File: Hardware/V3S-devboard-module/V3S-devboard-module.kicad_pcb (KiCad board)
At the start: 4 copper layers, 31.9 x 52.9 mm, 84 parts, among them J101 Conn_01x02, J201 Micro_SD_Card_Det1, J301 AS0BC21-S30BE-7H, SW201 SW_MEC_5E, U101 EA3036C, U102 XC6206PxxxMR, U201 V3S, U202 W25Q128JVS, Y201 Crystal_Small, Y202 Crystal_GND24_Small

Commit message: started working on exp board
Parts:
- moved J101 153.1 mm to (6.64, 2.68)
- moved C103 148.6 mm to (21.5, 15.2)
- moved C104 148.6 mm to (21.5, 13.5)
- moved C105 148.6 mm to (25.7, 18.0)
- moved C108 148.6 mm to (21.5, 10.5)
- moved C109 148.6 mm to (20.4, 8.68)
- moved C111 148.6 mm to (26.4, 8.57)
- moved C202 148.6 mm to (24.4, 34.8)
- moved C203 148.6 mm to (19.0, 30.5)
- moved C204 148.6 mm to (20.1, 31.6)
- moved C207 148.6 mm to (20.8, 32.9)
- moved C208 148.6 mm to (18.4, 36.8)
- moved C210 148.6 mm to (16.8, 34.4)
- moved C211 148.6 mm to (16.1, 33.7)
- moved C213 148.6 mm to (12.5, 41.0)
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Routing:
- net 5V: track 41.3 -> 45.0 mm
- net 1V2: track 179.8 -> 178.9 mm
- net GND: vias 54 -> 95
- net (no net): vias 1 -> 0
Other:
- board size 31.9 x 52.9 mm -> 32 x 55 mm

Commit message: working on final touches
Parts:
- added D101: LED, LED_SMD:LED_0603_1608Metric, F.Cu at (25.2, 2.27)
- added R108: 1K, Resistor_SMD:R_0402_1005Metric, B.Cu at (27.8, 2.27)
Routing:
- net Net-(D101-A): track 0.00 -> 2.82 mm, vias 0 -> 1
- net 5V: vias 38 -> 39
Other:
- board text added: "AM 2k24"
- board text added: "V3S Devboard"

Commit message: Minor changes. Sent to fab
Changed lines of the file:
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@@
 	)
 	(via
-		(at 19.138119 36.036881)
+		(at 19.3 35.9)
 		(size 0.5)
 		(drill 0.3)
@@
 		(start 10.275 39.875)
 		(end 8.925 39.875)
+		(width 0.5)
+		(layer "In1.Cu")
+		(net 2)
+	)
+	(segment
+		(start 13.325 41.85)
+		(end 9.475 41.85)
+		(width 0.5)
+		(layer "In1.Cu")
+		(net 2)
+	)
+	(segment
+		(start 19.275 35.9)
+		(end 13.325 41.85)
 		(width 0.5)
 		(layer "In1.Cu")
@@
 	)
 	(segment
-		(start 8.125 40.5)
-		(end 9.475 41.85)
+		(start 9.475 41.85)
+		(end 8.125 40.5)
 		(width 0.5)
 		(layer "In1.Cu")
@@
 	)
 	(segment
-		(start 7.575 40.5)
-		(end 2.9 35.825)
+		(start 19.3 35.9)
+		(end 19.275 35.9)
 		(width 0.5)
 		(layer "In1.Cu")
@@
 	)
 	(segment
-		(start 13.325 41.85)
-		(end 19.138119 36.036881)
+		(start 7.575 40.5)
+		(end 2.9 35.825)
 		(width 0.5)
 		(layer "In1.Cu")
@@
 		(width 0.5)
 		(layer "In1.Cu")
-		(net 2)
-	)
-	(segment
-		(start 9.475 41.85)
-		(end 13.325 41.85)
-		(width 0.5)
-		(layer "In1.Cu")

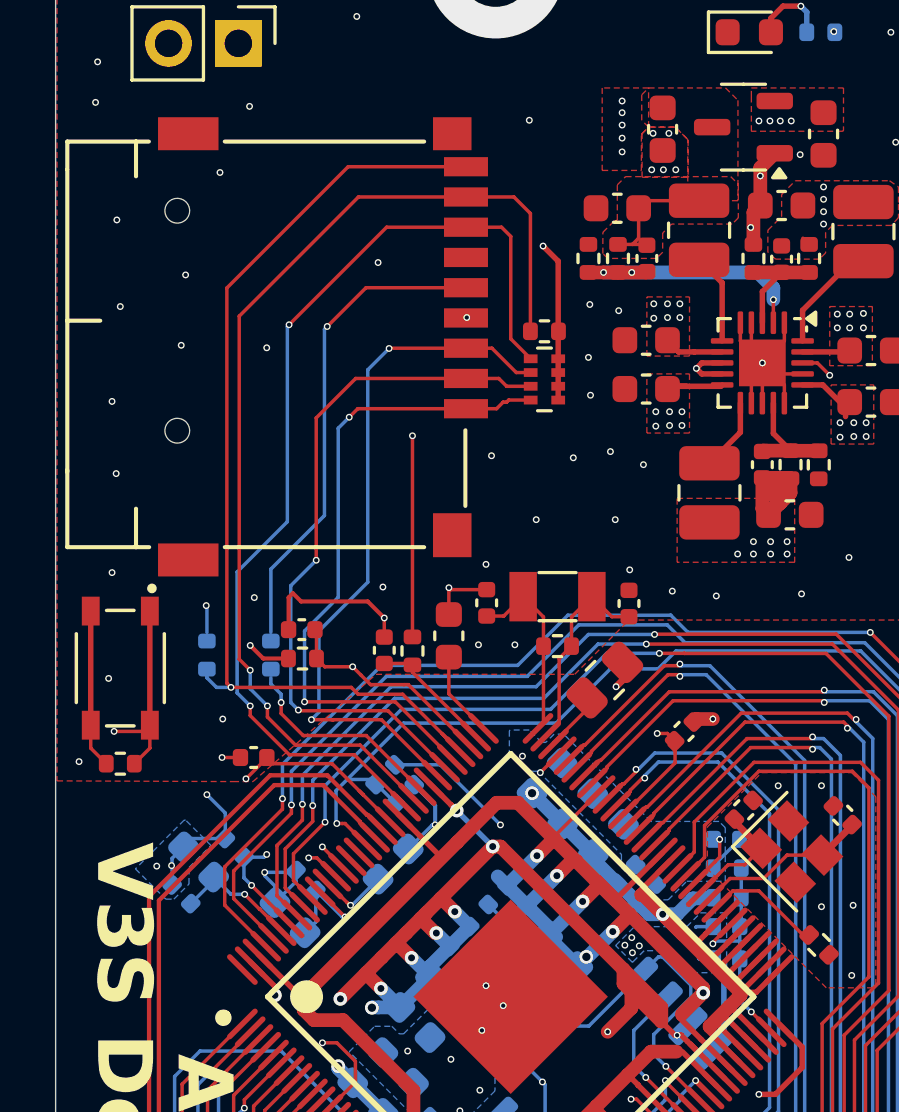
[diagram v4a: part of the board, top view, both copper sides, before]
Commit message: fixed clearance problems, sent to fab
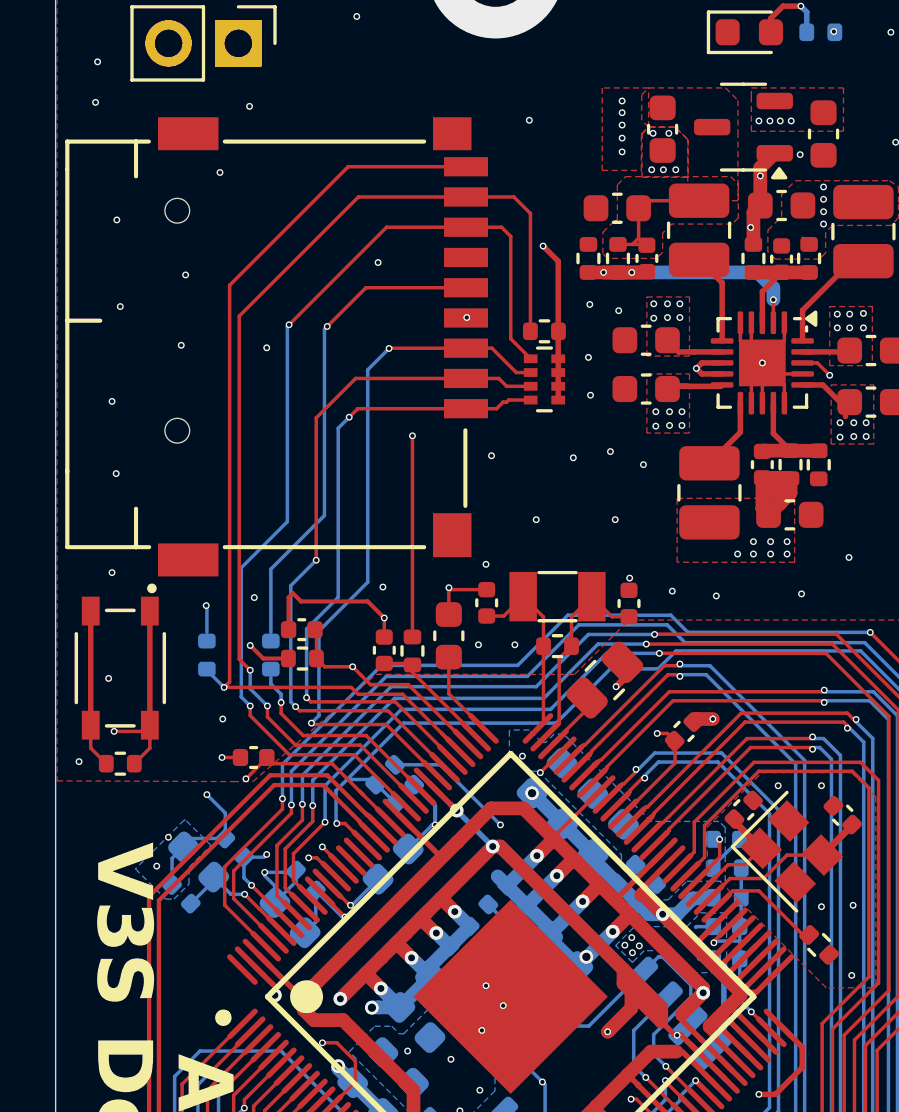
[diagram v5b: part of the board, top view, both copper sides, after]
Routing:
- net 1V8: track 61.8 -> 68.7 mm

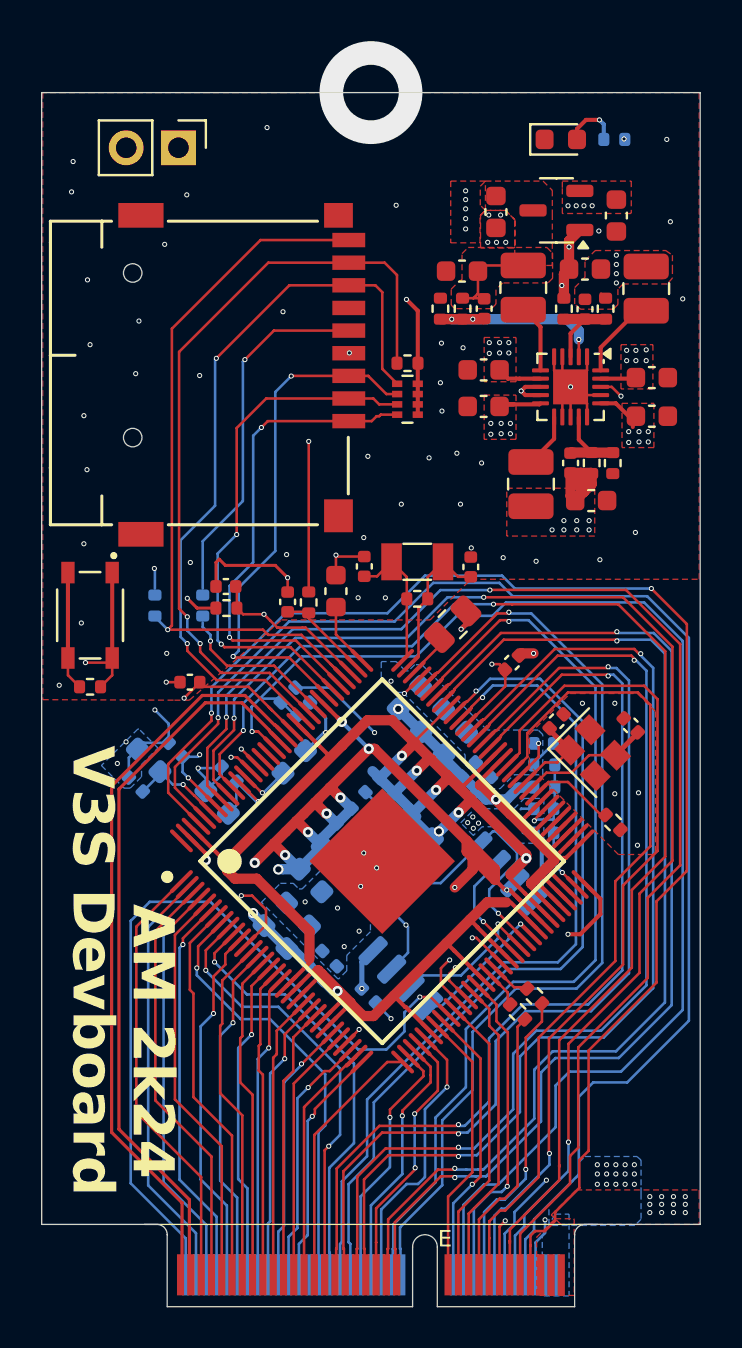
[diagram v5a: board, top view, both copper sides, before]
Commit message: changed clearances for devboard, sent to fab
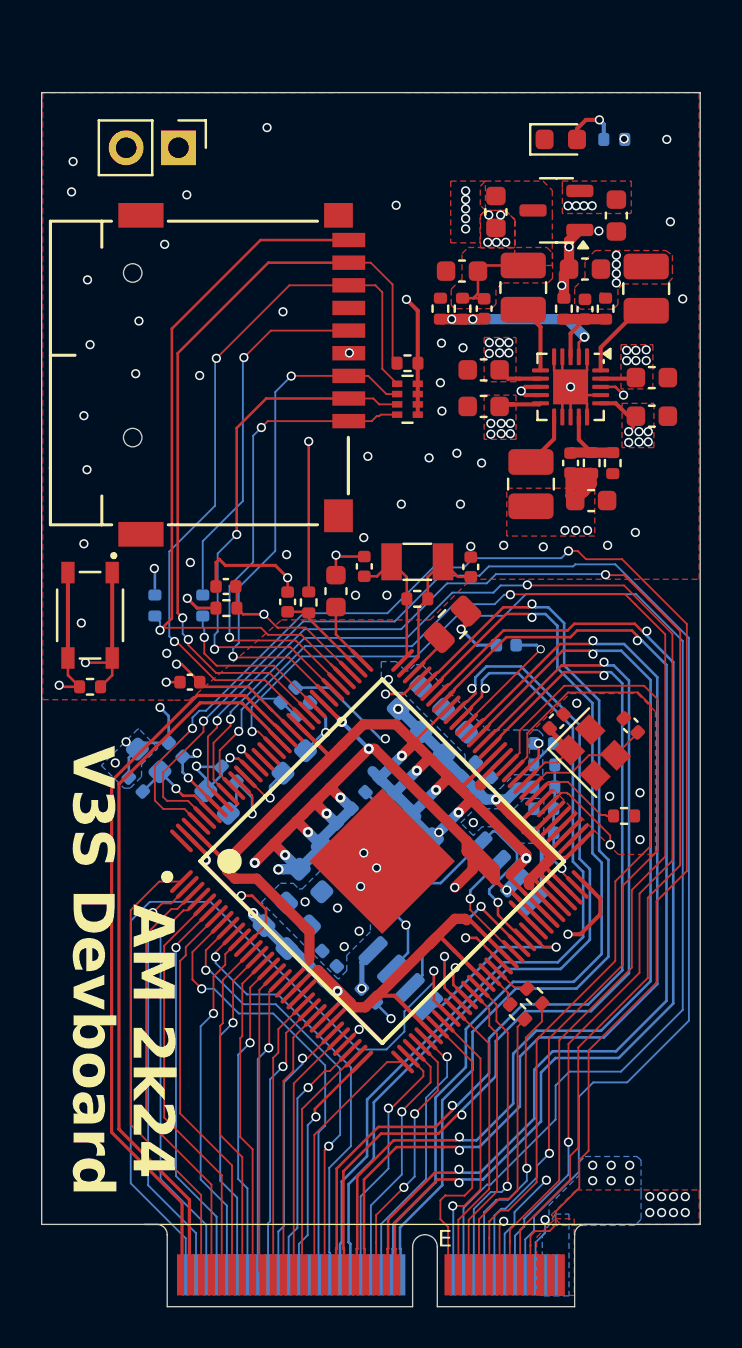
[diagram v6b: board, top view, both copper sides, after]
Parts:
- C221: moved to B.Cu
- moved C221 0.89 mm to (22.6, 26.9), turned to 0 degrees
- moved R205 0.62 mm to (28.3, 35.1), turned to 0 degrees
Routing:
- net 3V3: track 178.6 -> 185.6 mm
- net SVREF: track 8.42 -> 13.9 mm
- net SPI.MOSI: track 6.93 -> 9.61 mm
- net GND: track 53.4 -> 55.9 mm, vias 95 -> 80
- net RESET: track 59.8 -> 62.2 mm
- net USB.USB_ID: track 39.1 -> 41.3 mm
- net ADCDAC.HPCOM: track 69.5 -> 71.4 mm
- net ADCDAC.HPCOMFB: track 68.9 -> 70.4 mm
- net ETH0.TX_N: track 45.4 -> 46.6 mm
- net ETH0.TX_P: track 46.2 -> 47.4 mm
- net CSI.MCSI_CK_N: track 41.0 -> 42.1 mm
- net CSI.MCSI_CK_P: track 40.1 -> 41.3 mm
- net SPI.CLK: track 7.47 -> 8.52 mm
- net VRA2: track 4.45 -> 5.36 mm
- net UART2.TX: track 13.2 -> 14.1 mm
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
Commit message: sent to fab... again
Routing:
- net 1V2: track 177.8 -> 181.1 mm, vias 13 -> 14
- net 1V8: track 68.8 -> 69.8 mm
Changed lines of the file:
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@@
 	)
 	(segment
-		(start 24.04334 40.602691)
-		(end 22.788225 39.347577)
-		(width 0.2)
-		(layer "F.Cu")
-		(net 2)
-	)
-	(segment
 		(start 24.609025 40.037006)
 		(end 23.477654 38.905635)
@@
 	)
 	(segment
+		(start 22.775 39.8)
+		(end 22.775 39.825)
+		(width 0.2)
+		(layer "F.Cu")
+		(net 2)
+	)
+	(segment
 		(start 21.497755 43.148276)
 		(end 20.048187 41.698707)
@@
 	)
 	(segment
+		(start 24.04334 40.602691)
+		(end 23.007824 39.567176)
+		(width 0.2)
+		(layer "F.Cu")
+		(net 2)
+	)
+	(segment
 		(start 22.063441 32.11741)
 		(end 20.348707 33.832144)
@@
 	)
 	(segment
+		(start 23.007824 39.567176)
+		(end 22.775 39.8)
+		(width 0.2)
+		(layer "F.Cu")
+		(net 2)
+	)
+	(segment
 		(start 18.825 41.4)
 		(end 18.9875 41.2375)
@@
 	)
 	(via
+		(at 22.775 39.825)
+		(size 0.45)
+		(drill 0.3)
+		(layers "F.Cu" "B.Cu")
+		(net 2)
+	)
+	(via
 		(at 20.260319 34.981192)
 		(size 0.5)
@@
 	)
 	(segment
+		(start 23.85 40.9)
+		(end 25.573 40.9)
+		(width 0.2)
+		(layer "B.Cu")
+		(net 2)
+	)
+	(segment
 		(start 18.987526 36.253984)
 		(end 20.260319 34.981192)
@@
 	)
 	(segment
+		(start 22.775 39.825)
+		(end 23.85 40.9)
+		(width 0.2)
+		(layer "B.Cu")
+		(net 2)
+	)
+	(segment
 		(start 16.410122 33.315956)
 		(end 17.502602 32.223476)
@@
 	)
 	(segment
-		(start 21.374012 33.655367)
-		(end 21.303301 33.655367)
-		(width 0.5)
-		(layer "F.Cu")
-		(net 6)
-	)
-	(segment
 		(start 24.891868 39.754163)
 		(end 23.672109 38.534404)
@@
 	)
 	(segment
+		(start 21.380367 33.655367)
+		(end 22.075 34.35)
+		(width 0.5)
+		(layer "F.Cu")
+		(net 6)
+	)
+	(segment
 		(start 24.909546 37.190901)
 		(end 24.87419 37.190901)
@@
 	)
 	(segment
+		(start 21.374012 33.584656)
+		(end 21.303301 33.655367)
+		(width 0.5)
+		(layer "F.Cu")
+		(net 6)
+	)
+	(segment
 		(start 24.326183 34.380152)
 		(end 23.654431 35.051903)
@@
 	)
 	(segment
-		(start 21.374012 33.584656)
-		(end 21.303301 33.655367)
+		(start 25.7 18.479997)
+		(end 26.2 18.479997)
 		(width 0.5)
 		(layer "F.Cu")
@@
 	)
 	(segment
-		(start 25.7 18.479997)
-		(end 26.2 18.479997)
+		(start 21.303301 33.655367)
+		(end 21.380367 33.655367)
 		(width 0.5)
 		(layer "F.Cu")
@@
 	)
 	(segment
+		(start 10.748008 47.701992)
+		(end 10.748008 57.45)
+		(width 0.09)
+		(layer "F.Cu")
+		(net 68)
+	)
+	(segment
 		(start 11.315418 42.865433)
 		(end 10.575 43.605851)
@@
 	)
 	(segment
-		(start 10.575 43.605851)
-		(end 10.575 57.276992)
+		(start 10.875 47.575)
+		(end 10.748008 47.701992)
 		(width 0.09)
 		(layer "F.Cu")
@@
 	)
 	(segment
-		(start 10.575 57.276992)
-		(end 10.748008 57.45)
+		(start 10.575 47.275)
+		(end 10.875 47.575)
+		(width 0.09)
+		(layer "F.Cu")
+		(net 68)
+	)
+	(segment
+		(start 10.575 43.605851)
+		(end 10.575 47.275)
 		(width 0.09)
 		(layer "F.Cu")
@@
 	)
 	(segment
-		(start 9.825 12.875)
-		(end 9.775 12.925)
+		(start 9.775 19.85)
+		(end 7.825 21.8)
 		(width 0.09)
 		(layer "B.Cu")
@@
 	(segment
 		(start 7.825 21.8)
-		(end 7.825 24.1)
+		(end 7.825 24.415)
 		(width 0.09)
 		(layer "B.Cu")
@@
 	)
 	(segment
-		(start 9.775 19.85)
-		(end 7.825 21.8)
+		(start 9.825 12.875)
+		(end 9.775 12.925)
 		(width 0.09)
 		(layer "B.Cu")
@@
 		(layer "B.Cu")
 		(hatch edge 0.5)
+		(priority 21)
+		(connect_pads yes
+			(clearance 0.127)
+		)
+		(min_thickness 0.25)
+		(filled_areas_thickness no)
+		(fill yes
+			(thermal_gap 0.5)
+			(thermal_bridge_width 0.5)
+		)
+		(polygon
+			(pts
+				(xy 12.425 29.55) (xy 12.9 29.075) (xy 13.25 29.075) (xy 14.125 29.95) (xy 14.125 31.525) (xy 12.85 32.8)
+				(xy 12.7 32.8) (xy 11.975 32.075) (xy 11.975 31.825) (xy 13.025 30.775) (xy 13.025 30.325) (xy 12.425 29.725)
+			)
+		)
+	)
+	(zone
+		(net 30)
+		(net_name "GND")
+		(layer "B.Cu")
+		(hatch edge 0.5)
 		(priority 13)
 		(connect_pads yes
@@
 			)
 		)
+	)
+	(zone
+		(net 30)
+		(net_name "GND")
+		(layer "B.Cu")
+		(hatch edge 0.5)
+		(priority 20)
+		(connect_pads yes
+			(clearance 0.127)
+		)
+		(min_thickness 0.25)
+		(filled_areas_thickness no)
+		(fill yes
+			(thermal_gap 0.5)
+			(thermal_bridge_width 0.5)
+		)
+		(polygon
+			(pts
+				(xy 7.425 32.325) (xy 6.975 32.775) (xy 6.975 33.125) (xy 7.225 33.375) (xy 7.225 34.025) (xy 8.05 34.85)
+				(xy 8.15 34.85) (xy 8.775 34.225) (xy 8.775 33.475) (xy 8.725 33.425) (xy 8.725 33.375) (xy 9.6 32.5)
+				(xy 9.6 32.325) (xy 9.1 31.825) (xy 8.275 31.825) (xy 7.65 32.45) (xy 7.525 32.325)
+			)
+		)

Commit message: Minor changed. Final version sent to fab (really)
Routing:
- net USB.USB_ID: track 41.3 -> 42.1 mm
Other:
- board text added: "5V"
- board text added: "PWR"
